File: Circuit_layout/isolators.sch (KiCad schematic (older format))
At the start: 29 parts, among them U17 MCP6004, U19 ACPL-C870, U20 ACPL-C870, U21 MCP6001

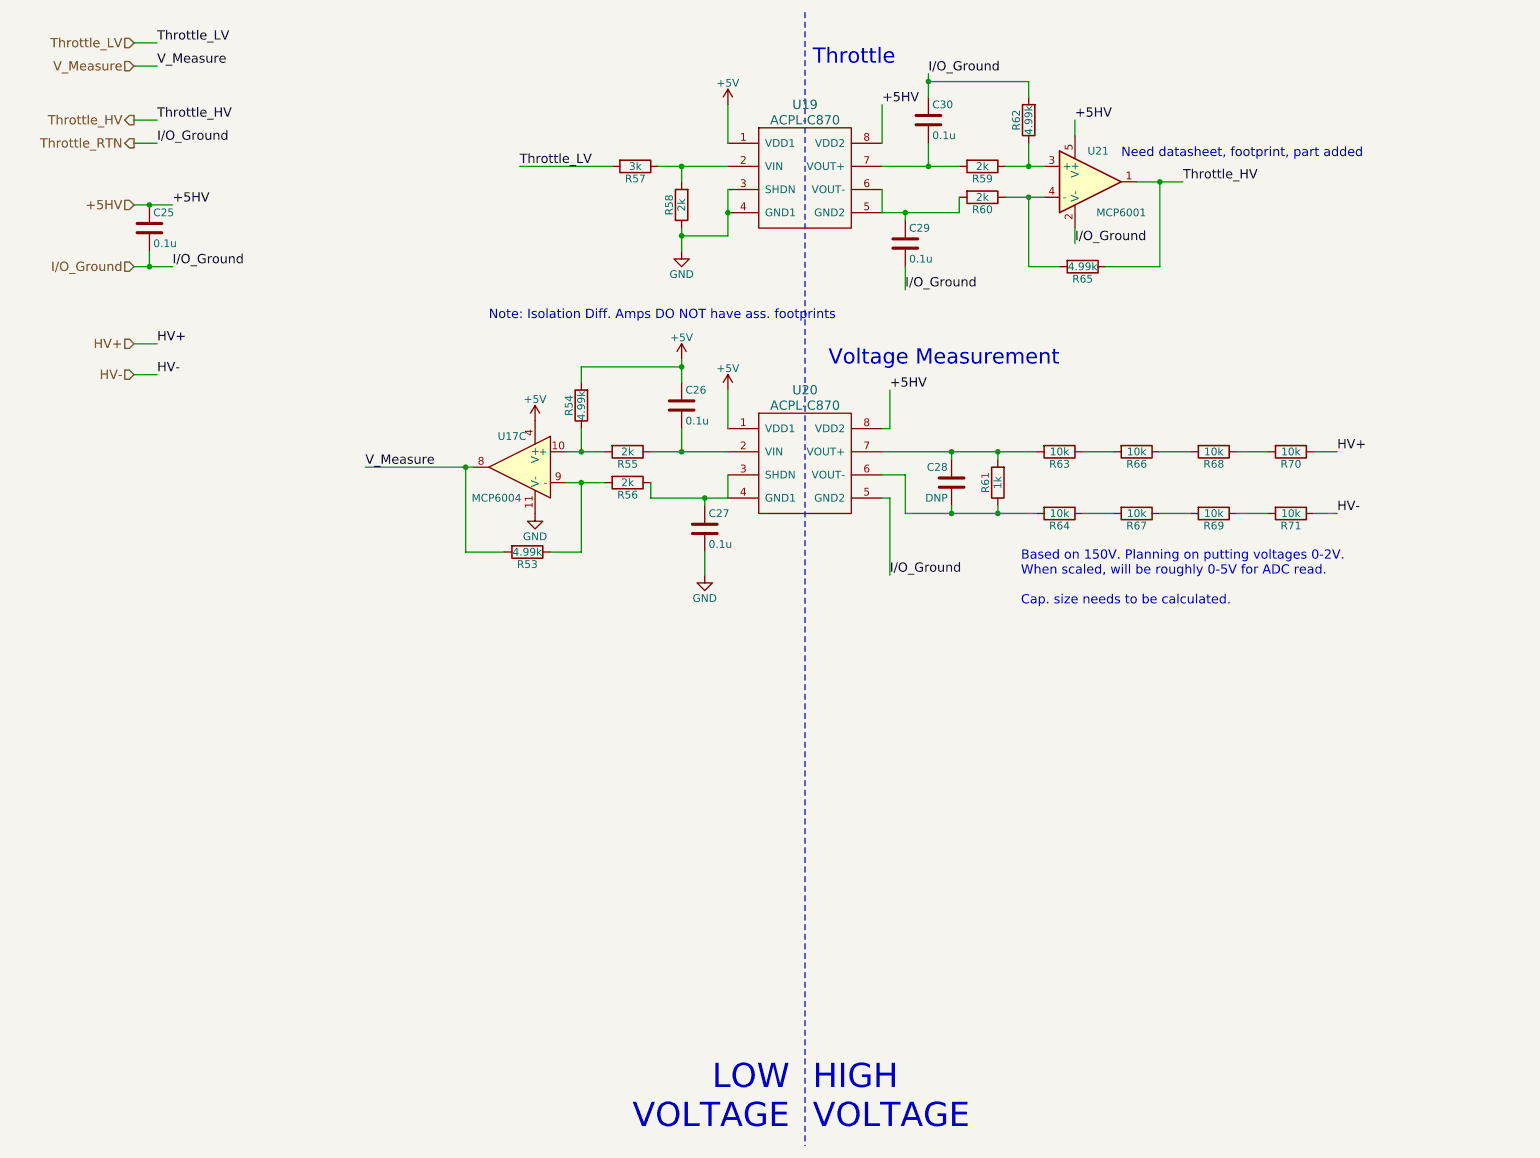
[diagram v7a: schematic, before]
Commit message: cleaned up sch, added bypass pass. no net warnings
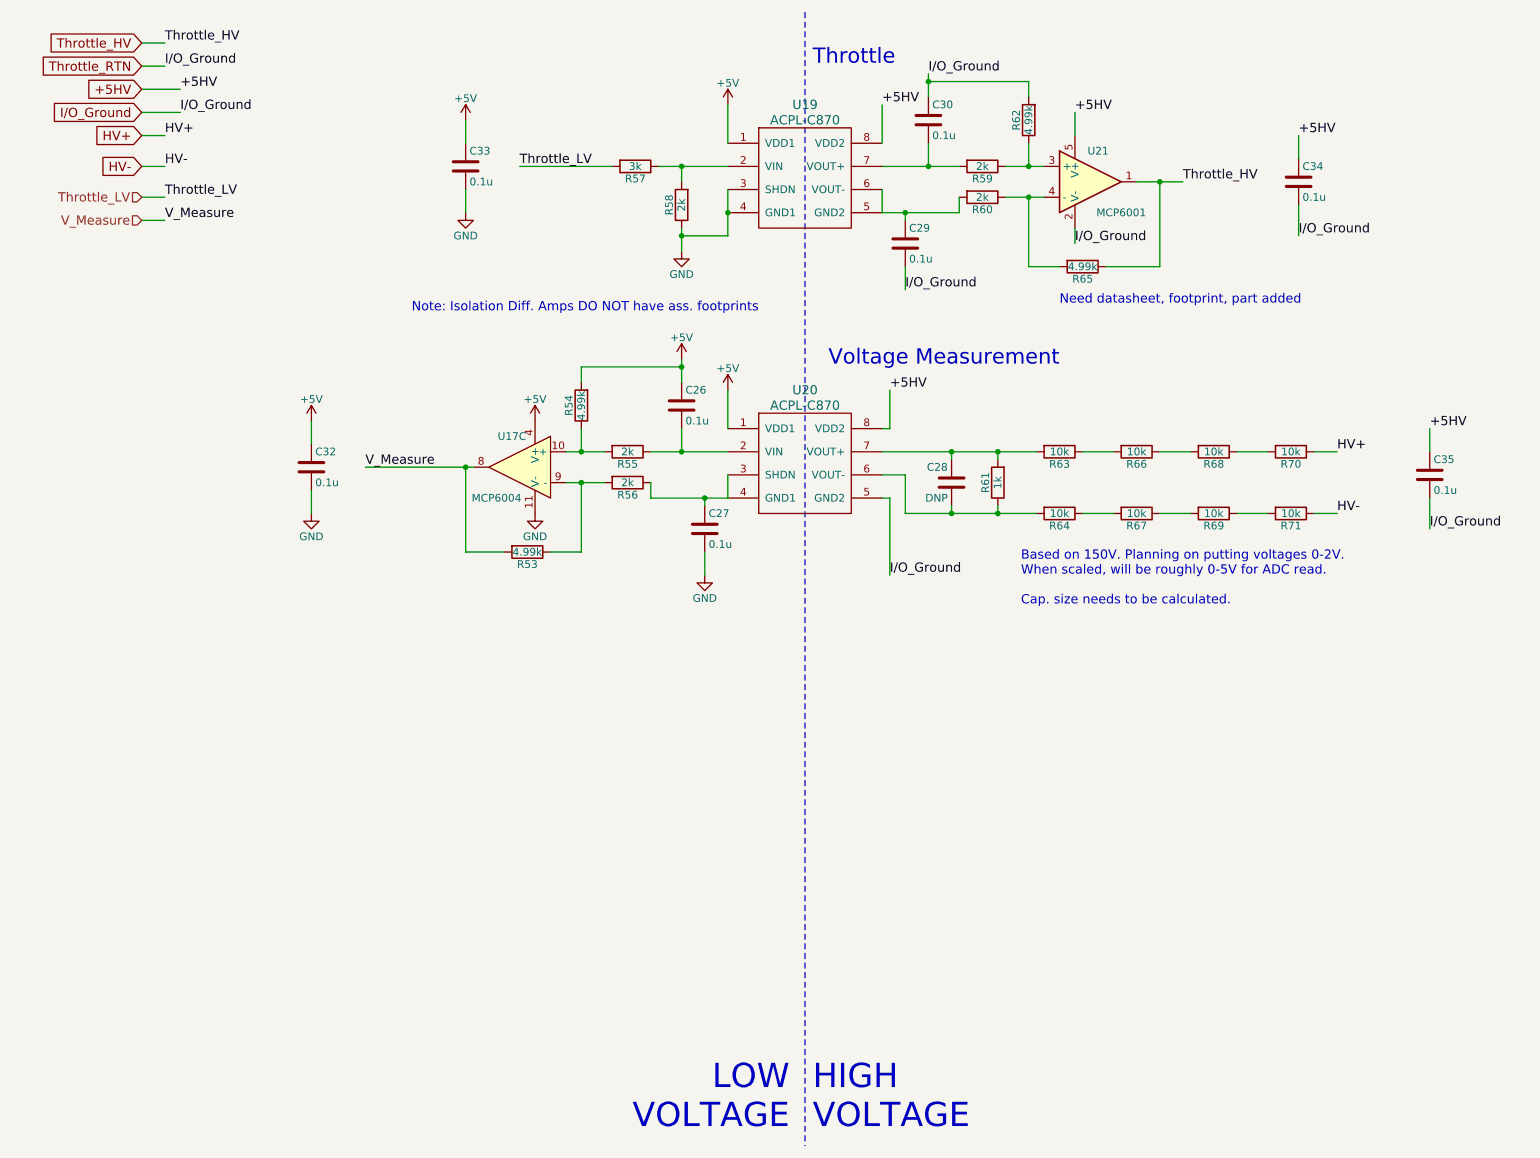
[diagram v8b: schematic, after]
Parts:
- removed C25: 0.1u, Capacitors_SMD:C_0805_HandSoldering, symbol C
- added C32, C33, C34, C35: 0.1u, Capacitors_SMD:C_0805_HandSoldering, symbol C
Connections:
- net +5HV: now also C34.1, C35.1
- net +5V: now also C32.1, C33.1
- net GND: now also C32.2, C33.2
- net I/O_Ground: now also C34.2, C35.2
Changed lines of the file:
@@
 EESchema Schematic File Version 2
 LIBS:Circuit_layout-rescue
-LIBS:TSI_KiCad_Lib
 LIBS:TSI_HV_Isolater-cache
 LIBS:74xgxx
@@
 Wire Wire Line
 	4950 1600 4950 1900
-Text Label 7200 1150 0    60   ~ 0
+Text Label 7200 1100 0    60   ~ 0
 +5HV
 Text Label 7200 1950 0    60   ~ 0
@@
 Text Label 2600 3400 0    60   ~ 0
 V_Measure
-Text HLabel 1100 650  0    60   Input ~ 0
+Text HLabel 1150 1650 0    60   Input ~ 0
 Throttle_LV
-Text HLabel 1100 1700 0    60   Input ~ 0
-+5HV
-Text HLabel 1100 2600 0    60   Input ~ 0
-HV+
-Text HLabel 1100 2800 0    60   Input ~ 0
-HV-
-Text HLabel 1100 1150 0    60   Output ~ 0
-Throttle_HV
-Text HLabel 1100 800  0    60   Input ~ 0
+Text HLabel 1150 1800 0    60   Input ~ 0
 V_Measure
 Wire Wire Line
@@
 	3250 3950 3500 3950
 $Comp
-L +5V #PWR093
+L +5V #PWR116
 U 1 1 58B246C4
 P 4650 2700
-F 0 "#PWR093" H 4650 2550 50  0001 C CNN
+F 0 "#PWR116" H 4650 2550 50  0001 C CNN
 F 1 "+5V" H 4650 2840 50  0000 C CNN
 F 2 "" H 4650 2700 50  0000 C CNN
@@
 $EndComp
 $Comp
-L +5V #PWR094
+L +5V #PWR119
 U 1 1 58B24710
 P 4950 2900
-F 0 "#PWR094" H 4950 2750 50  0001 C CNN
+F 0 "#PWR119" H 4950 2750 50  0001 C CNN
 F 1 "+5V" H 4950 3040 50  0000 C CNN
 F 2 "" H 4950 2900 50  0000 C CNN
@@
 $EndComp
 $Comp
-L +5V #PWR095
+L +5V #PWR113
 U 1 1 58B2475C
 P 3700 3100
-F 0 "#PWR095" H 3700 2950 50  0001 C CNN
+F 0 "#PWR113" H 3700 2950 50  0001 C CNN
 F 1 "+5V" H 3700 3240 50  0000 C CNN
 F 2 "" H 3700 3100 50  0000 C CNN
@@
 $EndComp
 $Comp
-L GND #PWR096
+L GND #PWR114
 U 1 1 58B247A8
 P 3700 3700
-F 0 "#PWR096" H 3700 3450 50  0001 C CNN
+F 0 "#PWR114" H 3700 3450 50  0001 C CNN
 F 1 "GND" H 3700 3550 50  0000 C CNN
 F 2 "" H 3700 3700 50  0000 C CNN
@@
 $EndComp
 $Comp
-L GND #PWR097
+L GND #PWR117
 U 1 1 58B2480E
 P 4800 4100
-F 0 "#PWR097" H 4800 3850 50  0001 C CNN
+F 0 "#PWR117" H 4800 3850 50  0001 C CNN
 F 1 "GND" H 4800 3950 50  0000 C CNN
 F 2 "" H 4800 4100 50  0000 C CNN
@@
 	4950 1900 4650 1900
 $Comp
-L GND #PWR098
+L GND #PWR115
 U 1 1 58B25770
 P 4650 2000
-F 0 "#PWR098" H 4650 1750 50  0001 C CNN
+F 0 "#PWR115" H 4650 1750 50  0001 C CNN
 F 1 "GND" H 4650 1850 50  0000 C CNN
 F 2 "" H 4650 2000 50  0000 C CNN
@@
 $EndComp
 $Comp
-L +5V #PWR099
+L +5V #PWR118
 U 1 1 58B257CF
 P 4950 1050
-F 0 "#PWR099" H 4950 900 50  0001 C CNN
+F 0 "#PWR118" H 4950 900 50  0001 C CNN
 F 1 "+5V" H 4950 1190 50  0000 C CNN
 F 2 "" H 4950 1050 50  0000 C CNN
@@
 $EndComp
 Wire Wire Line
-	1100 2800 1250 2800
-Wire Wire Line
-	1100 2600 1250 2600
-Wire Wire Line
-	1100 1150 1250 1150
-Wire Wire Line
-	1100 800  1250 800
-Wire Wire Line
-	1100 650  1250 650
-Text Label 1250 650  0    60   ~ 0
+	1150 1450 1300 1450
+Wire Wire Line
+	1150 1250 1300 1250
+Wire Wire Line
+	1150 650  1300 650
+Wire Wire Line
+	1150 1800 1300 1800
+Wire Wire Line
+	1150 1650 1300 1650
+Text Label 1300 1650 0    60   ~ 0
 Throttle_LV
-Text Label 1250 800  0    60   ~ 0
+Text Label 1300 1800 0    60   ~ 0
 V_Measure
-Text Label 1250 1150 0    60   ~ 0
+Text Label 1300 650  0    60   ~ 0
 Throttle_HV
-Text Label 1350 1700 0    60   ~ 0
+Text Label 1400 950  0    60   ~ 0
 +5HV
-Text Label 1250 2600 0    60   ~ 0
+Text Label 1300 1250 0    60   ~ 0
 HV+
-Text Label 1250 2800 0    60   ~ 0
+Text Label 1300 1450 0    60   ~ 0
 HV-
 Wire Wire Line
-	1100 1700 1350 1700
-Connection ~ 1200 1700
-Wire Wire Line
-	1200 2000 1200 2100
+	1150 950  1400 950
 $Comp
 L R R64
@@
 $EndComp
 $Comp
-L C C25
-U 1 1 58B44F65
-P 1200 1850
-F 0 "C25" H 1225 1950 50  0000 L CNN
-F 1 "0.1u" H 1225 1750 50  0000 L CNN
-F 2 "Capacitors_SMD:C_0805_HandSoldering" H 1238 1700 50  0001 C CNN
-F 3 "http://www.kemet.com/Lists/ProductCatalog/Attachments/53/KEM_C1002_X7R_SMD.pdf" H 1200 1850 50  0001 C CNN
-F 4 "399-1168-1-ND" H 1200 1850 60  0001 C CNN "Digikey P/N"
-F 5 "http://www.digikey.com/product-detail/en/kemet/C0805C104K3RACTU/399-1168-1-ND/411443" H 1200 1850 60  0001 C CNN "URL"
-F 6 "C0805C104K3RACTU" H 1200 1850 60  0001 C CNN "Man P/N"
-	1    1200 1850
-	1    0    0    -1
-$EndComp
-$Comp
 L ACPL-C870 U19
 U 1 1 58B45431
@@
 	1    0    0    -1
 $EndComp
-Text Notes 3400 2450 0    60   ~ 0
+Text Notes 2900 2400 0    60   ~ 0
 Note: Isolation Diff. Amps DO NOT have ass. footprints
 $Comp
@@
 	-1   0    0    -1
 $EndComp
-Text Label 1350 2100 0    60   ~ 0
+Text Label 1400 1100 0    60   ~ 0
 I/O_Ground
 Text Label 6250 850  0    60   ~ 0
 I/O_Ground
-Connection ~ 1200 2100
-Wire Wire Line
-	1100 2100 1350 2100
-Text HLabel 1100 2100 0    60   Input ~ 0
+Wire Wire Line
+	1150 1100 1400 1100
+Wire Wire Line
+	1150 800  1300 800
+Text Label 1300 800  0    60   ~ 0
 I/O_Ground
-Text HLabel 1100 1300 0    60   Output ~ 0
-Throttle_RTN
-Wire Wire Line
-	1100 1300 1250 1300
-Text Label 1250 1300 0    60   ~ 0
-I/O_Ground
 Wire Wire Line
 	6900 2100 7100 2100
@@
 	7200 1950 7200 1850
 Wire Wire Line
-	7200 1150 7200 1250
+	7200 1100 7200 1250
 $Comp
 L MCP6001 U21
@@
 	1    0    0    -1
 $EndComp
-Text Notes 7500 1400 0    60   ~ 0
+Text Notes 7100 2350 0    60   ~ 0
 Need datasheet, footprint, part added
+$Comp
+L C C34
+U 1 1 58B8FF60
+P 8650 1550
+F 0 "C34" H 8675 1650 50  0000 L CNN
+F 1 "0.1u" H 8675 1450 50  0000 L CNN
+F 2 "Capacitors_SMD:C_0805_HandSoldering" H 8688 1400 50  0001 C CNN
+F 3 "http://www.kemet.com/Lists/ProductCatalog/Attachments/53/KEM_C1002_X7R_SMD.pdf" H 8650 1550 50  0001 C CNN
+F 4 "399-1168-1-ND" H 8650 1550 60  0001 C CNN "Digikey P/N"
+F 5 "http://www.digikey.com/product-detail/en/kemet/C0805C104K3RACTU/399-1168-1-ND/411443" H 8650 1550 60  0001 C CNN "URL"
+F 6 "C0805C104K3RACTU" H 8650 1550 60  0001 C CNN "Man P/N"
+	1    8650 1550
+	1    0    0    -1
+$EndComp
+Text Label 8650 1900 0    60   ~ 0
+I/O_Ground
+Text Label 8650 1250 0    60   ~ 0
++5HV
+Wire Wire Line
+	8650 1900 8650 1700
+Wire Wire Line
+	8650 1400 8650 1250
+$Comp
+L C C33
+U 1 1 58B9348B
+P 3250 1450
+F 0 "C33" H 3275 1550 50  0000 L CNN
+F 1 "0.1u" H 3275 1350 50  0000 L CNN
+F 2 "Capacitors_SMD:C_0805_HandSoldering" H 3288 1300 50  0001 C CNN
+F 3 "http://www.kemet.com/Lists/ProductCatalog/Attachments/53/KEM_C1002_X7R_SMD.pdf" H 3250 1450 50  0001 C CNN
+F 4 "399-1168-1-ND" H 3250 1450 60  0001 C CNN "Digikey P/N"
+F 5 "http://www.digikey.com/product-detail/en/kemet/C0805C104K3RACTU/399-1168-1-ND/411443" H 3250 1450 60  0001 C CNN "URL"
+F 6 "C0805C104K3RACTU" H 3250 1450 60  0001 C CNN "Man P/N"
+	1    3250 1450
+	1    0    0    -1
+$EndComp
+$Comp
+L +5V #PWR111
+U 1 1 58B93547
+P 3250 1150
+F 0 "#PWR111" H 3250 1000 50  0001 C CNN
+F 1 "+5V" H 3250 1290 50  0000 C CNN
+F 2 "" H 3250 1150 50  0000 C CNN
+F 3 "" H 3250 1150 50  0000 C CNN
+	1    3250 1150
+	1    0    0    -1
+$EndComp
+$Comp
+L GND #PWR112
+U 1 1 58B935AF
+P 3250 1750
+F 0 "#PWR112" H 3250 1500 50  0001 C CNN
+F 1 "GND" H 3250 1600 50  0000 C CNN
+F 2 "" H 3250 1750 50  0000 C CNN
+F 3 "" H 3250 1750 50  0000 C CNN
+	1    3250 1750
+	1    0    0    -1
+$EndComp
+Wire Wire Line
+	3250 1750 3250 1600
+Wire Wire Line
+	3250 1300 3250 1150
+$Comp
+L C C32
+U 1 1 58B939A0
+P 2250 3400
+F 0 "C32" H 2275 3500 50  0000 L CNN
+F 1 "0.1u" H 2275 3300 50  0000 L CNN
+F 2 "Capacitors_SMD:C_0805_HandSoldering" H 2288 3250 50  0001 C CNN
+F 3 "http://www.kemet.com/Lists/ProductCatalog/Attachments/53/KEM_C1002_X7R_SMD.pdf" H 2250 3400 50  0001 C CNN
+F 4 "399-1168-1-ND" H 2250 3400 60  0001 C CNN "Digikey P/N"
+F 5 "http://www.digikey.com/product-detail/en/kemet/C0805C104K3RACTU/399-1168-1-ND/411443" H 2250 3400 60  0001 C CNN "URL"
+F 6 "C0805C104K3RACTU" H 2250 3400 60  0001 C CNN "Man P/N"
+	1    2250 3400
+	1    0    0    -1
+$EndComp
+$Comp
+L +5V #PWR109
+U 1 1 58B939A6
+P 2250 3100
+F 0 "#PWR109" H 2250 2950 50  0001 C CNN
+F 1 "+5V" H 2250 3240 50  0000 C CNN
+F 2 "" H 2250 3100 50  0000 C CNN
+F 3 "" H 2250 3100 50  0000 C CNN
+	1    2250 3100
+	1    0    0    -1
+$EndComp
+$Comp
+L GND #PWR110
+U 1 1 58B939AC
+P 2250 3700
+F 0 "#PWR110" H 2250 3450 50  0001 C CNN
+F 1 "GND" H 2250 3550 50  0000 C CNN
+F 2 "" H 2250 3700 50  0000 C CNN
+F 3 "" H 2250 3700 50  0000 C CNN
+	1    2250 3700
+	1    0    0    -1
+$EndComp
+Wire Wire Line
+	2250 3700 2250 3550
+Wire Wire Line
+	2250 3250 2250 3100
+$Comp
+L C C35
+U 1 1 58B93A5A
+P 9500 3450
+F 0 "C35" H 9525 3550 50  0000 L CNN
+F 1 "0.1u" H 9525 3350 50  0000 L CNN
+F 2 "Capacitors_SMD:C_0805_HandSoldering" H 9538 3300 50  0001 C CNN
+F 3 "http://www.kemet.com/Lists/ProductCatalog/Attachments/53/KEM_C1002_X7R_SMD.pdf" H 9500 3450 50  0001 C CNN
+F 4 "399-1168-1-ND" H 9500 3450 60  0001 C CNN "Digikey P/N"
+F 5 "http://www.digikey.com/product-detail/en/kemet/C0805C104K3RACTU/399-1168-1-ND/411443" H 9500 3450 60  0001 C CNN "URL"
+F 6 "C0805C104K3RACTU" H 9500 3450 60  0001 C CNN "Man P/N"
+	1    9500 3450
+	1    0    0    -1
+$EndComp
+Text Label 9500 3800 0    60   ~ 0
+I/O_Ground
+Text Label 9500 3150 0    60   ~ 0
++5HV
+Wire Wire Line
+	9500 3800 9500 3600
+Wire Wire Line
+	9500 3300 9500 3150
+Text GLabel 1150 1250 0    60   Input ~ 0
+HV+
+Text GLabel 1150 1450 0    60   Input ~ 0
+HV-
+Text GLabel 1150 1100 0    60   Input ~ 0
+I/O_Ground
+Text GLabel 1150 950  0    60   Input ~ 0
++5HV
+Text GLabel 1150 800  0    60   Input ~ 0
+Throttle_RTN
+Text GLabel 1150 650  0    60   Input ~ 0
+Throttle_HV
 $EndSCHEMATC
